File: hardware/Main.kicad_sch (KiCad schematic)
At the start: 23 parts, among them IC102 APDS-9306-065, IC103 BME688, M101 BL54L15, Q101 BSS84, SW101 JOIN, X102 DEBUG

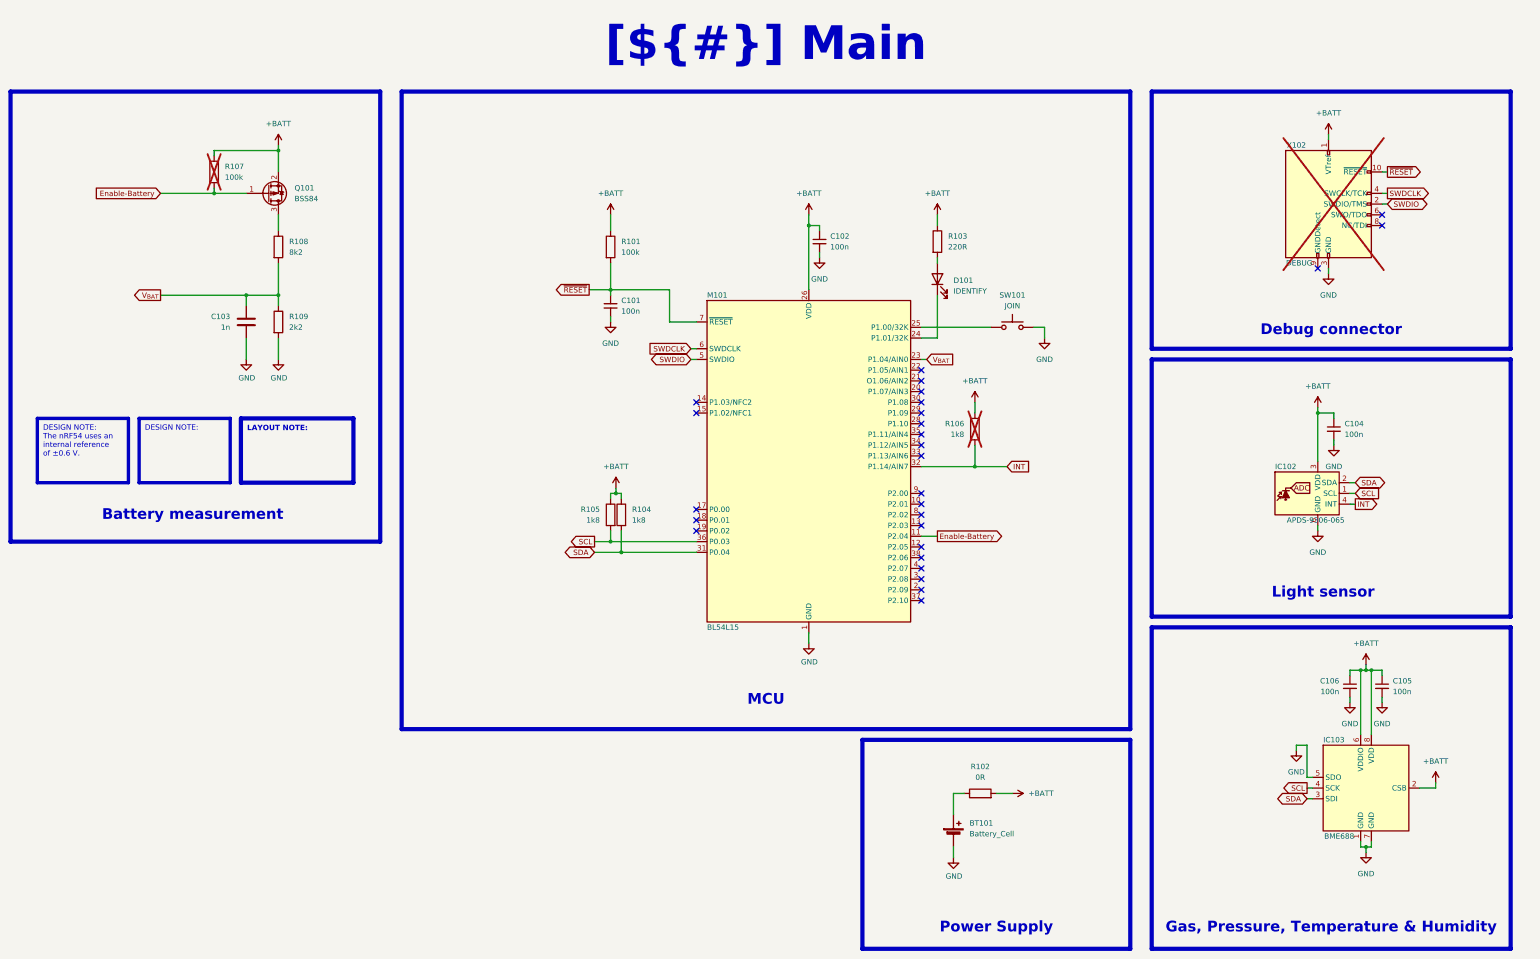
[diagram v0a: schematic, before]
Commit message: Feature: Issue #28
- Switch from CR2032 to CR2477 batteries for longer runtime

Closes #28

Signed-off-by: Daniel Kampert <DanielKampert@kampis-elektroecke.de>
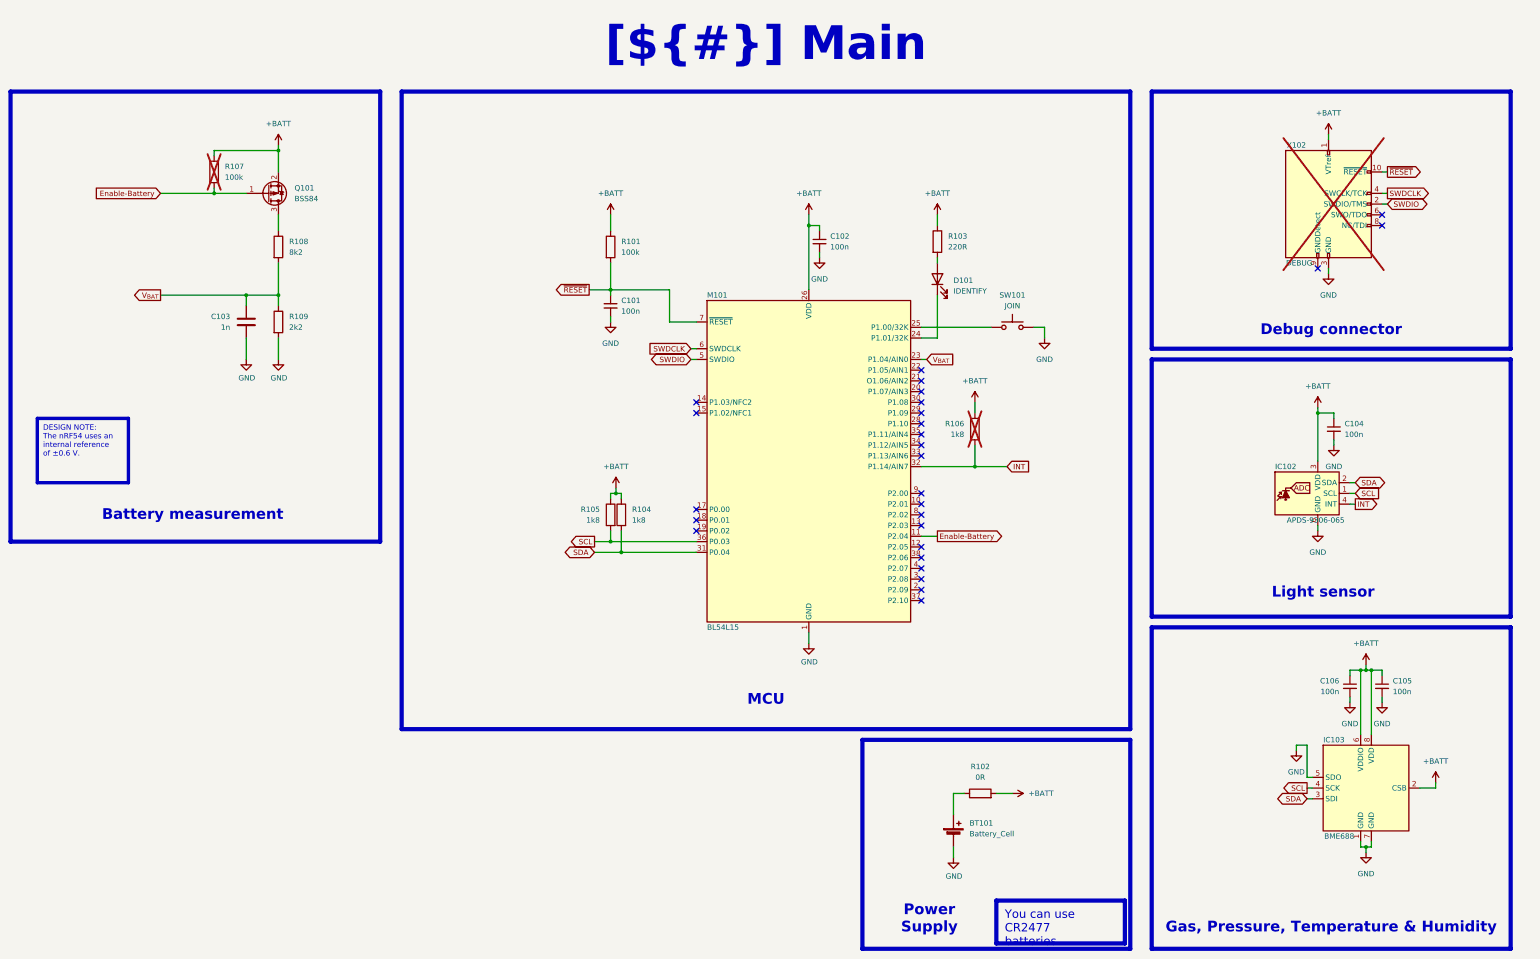
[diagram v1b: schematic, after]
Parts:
- BT101: footprint Keystone:3002 -> Keystone:3039; manf# 3002 -> 3039; mouser# 534-3002 -> 534-3039
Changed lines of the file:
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@@
 		(exclude_from_sim no)
 		(at 233.68 229.87 0)
-		(size 60.96 9.525)
+		(size 29.21 9.525)
 		(margins 1.9049 1.9049 1.9049 1.9049)
 		(stroke
@@
 		)
 	)
-	(text_box "DESIGN NOTE:"
+	(text_box "You can use CR2477 batteries."
 		(exclude_from_sim no)
-		(at 60.96 115.57 0)
-		(size 21.59 15.24)
-		(margins 1.3525 1.3525 1.3525 1.3525)
-		(stroke
-			(width 0.8)
+		(at 264.16 229.87 0)
+		(size 30.48 10.16)
+		(margins 2 2 2 2)
+		(stroke
+			(width 1)
 			(type solid)
-			(color 255 165 0 1)
+			(color 200 200 200 1)
 		)
 		(fill
@@
 			(font
 				(face "Arial")
-				(size 1.27 1.27)
+				(size 2 2)
 				(color 0 0 0 1)
-			)
-			(justify left top)
-		)
-	)
-	(text_box "LAYOUT NOTE:"
-		(exclude_from_sim no)
-		(at 85.09 115.57 0)
-		(size 26.67 15.24)
-		(margins 1.4525 1.4525 1.4525 1.4525)
-		(stroke
-			(width 1)
-			(type solid)
-			(color 0 0 255 1)
-		)
-		(fill
-			(type none)
-		)
-		(effects
-			(font
-				(face "Arial")
-				(size 1.27 1.27)
-				(thickness 0.4)
-				(bold yes)
-				(color 0 0 255 1)
 			)
 			(justify left top)
@@
 			)
 		)
-		(property "Footprint" "Keystone:3002"
+		(property "Footprint" "Keystone:3039"
 			(at 254 213.106 90)
 			(effects
@@
 			)
 		)
-		(property "Datasheet" "https://eu.mouser.com/datasheet/2/215/002-745381.pdf"
+		(property "Datasheet" "https://www.mouser.de/datasheet/3/201/1/3039.pdf"
 			(at 254 213.106 90)
 			(effects
@@
 			)
 		)
-		(property "manf#" "3002"
+		(property "manf#" "3039"
 			(at 254 214.63 0)
 			(effects
@@
 			)
 		)
-		(property "mouser#" "534-3002"
+		(property "mouser#" "534-3039"
 			(at 254 214.63 0)
 			(effects
